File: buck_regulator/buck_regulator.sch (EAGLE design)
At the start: 12 parts

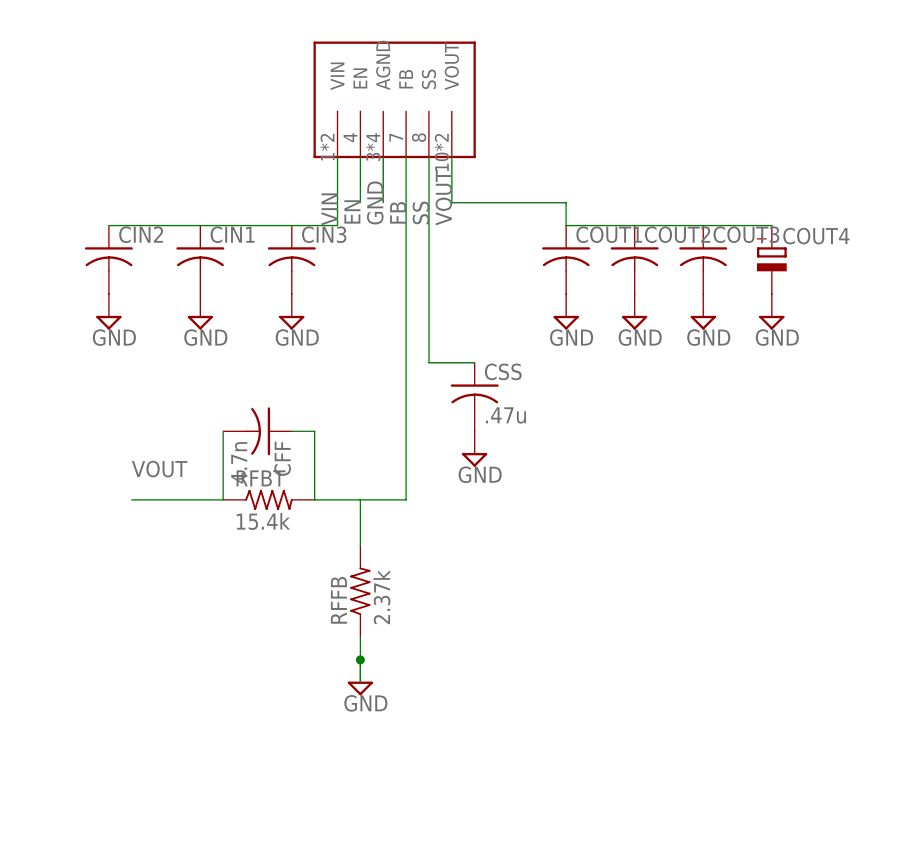
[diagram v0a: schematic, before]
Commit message: buck_regulator: re-route for revision B
Change-Id: Ie95bbfd6e64e4db471db740f6a7ad1b08f6b97fa
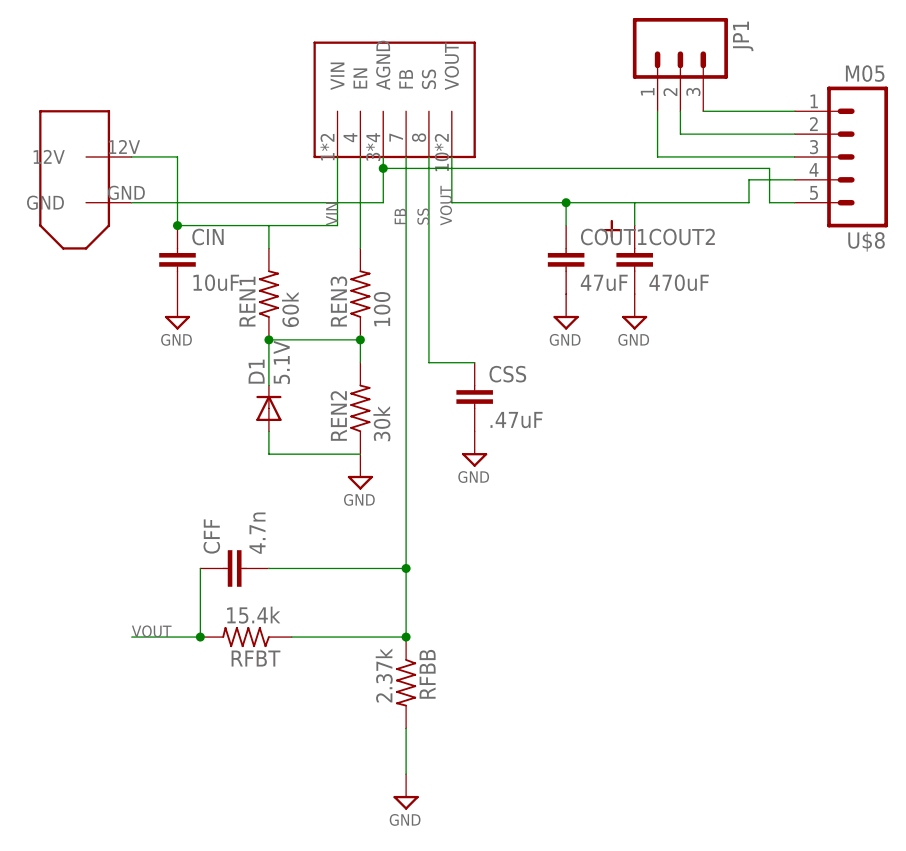
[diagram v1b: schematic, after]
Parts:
- removed CIN1, CIN2, CIN3: (no value), resistor:C-USC1206
- removed COUT3: (no value), resistor:C-USC1812K
- removed COUT4: (no value), resistor:CPOL-EU153CLV-1014
- removed RFFB: 2.37k, resistor:R-US_M0805
- added CIN: 10uF, pie:CAP0603-CAP
- added D1: 5.1V, SparkFun:DIODESOD
- added JP1: (no value), pie:M03MTA1X3
- added REN1: 60k, pie:R-US_R0603
- added REN2: 30k, pie:R-US_R0603
- added REN3: 100, pie:R-US_R0603
- added RFBB: 2.37k, pie:R-US_R0603
- added U$2: XT60CONNECTOR, pie:XT60CONNECTOR
- added U$8: M05, pie:M05
- CFF: device resistor:C-USC0805K -> pie:CAP0603-CAP
- COUT1: value (none) -> 47uF; device resistor:C-USC1206 -> SparkFun:CAP1206
- COUT2: value (none) -> 470uF; device resistor:C-USC1812K -> TANT_CASE_E:TANT_CASE_E
- CSS: value .47u -> .47uF; device resistor:C-USC0805K -> pie:CAP0603-CAP
- RFBT: device resistor:R-US_M0805 -> pie:R-US_R0603
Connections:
- removed net EN: U$1.EN
- new net N$1: REN3.2, U$1.EN
- new net N$2: JP1.1, U$8.3
- new net N$3: D1.C, REN1.1, REN2.2, REN3.1
- new net N$4: JP1.2, U$8.2
- new net N$5: JP1.3, U$8.1
- net FB: now also CFF.2, RFBB.1, RFBT.1; no longer CFF.1, RFBT.2, RFFB.2
- net GND: now also CIN.2, COUT2.NEG, D1.A, REN2.1, RFBB.2, U$2.GND, U$8.5; no longer CIN1.2, CIN2.2, CIN3.2, COUT2.2, COUT3.2, COUT4.-, RFFB.1
- net VIN: now also CIN.1, REN1.2, U$2.12V; no longer CIN1.1, CIN2.1, CIN3.1
- net VOUT: now also CFF.1, COUT2.POS, RFBT.2, U$8.4; no longer CFF.2, COUT2.1, COUT3.1, COUT4.+, RFBT.1
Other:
- moved on the sheet: CFF, RFBT

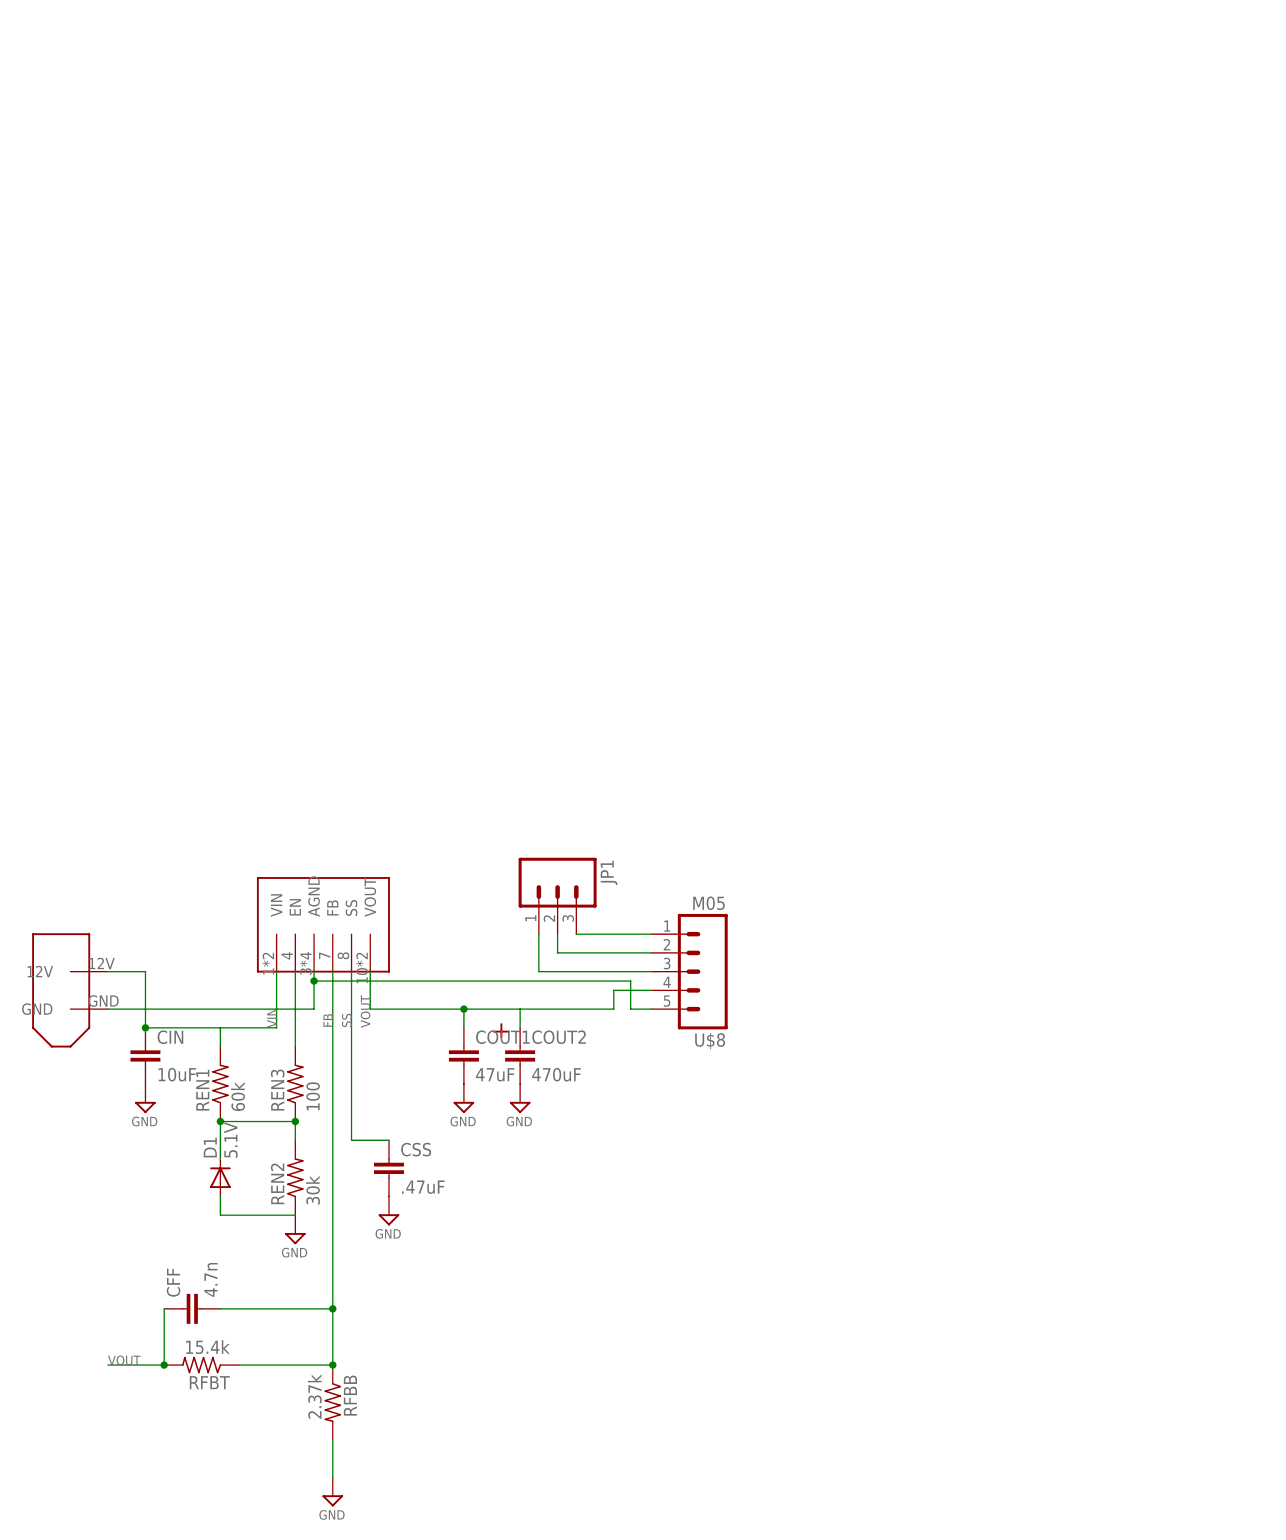
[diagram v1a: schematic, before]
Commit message: Fix all schematics to have a frame and be in quadrant I
Change-Id: I9709ffe2e940512e8f74172f888a837b658cad74
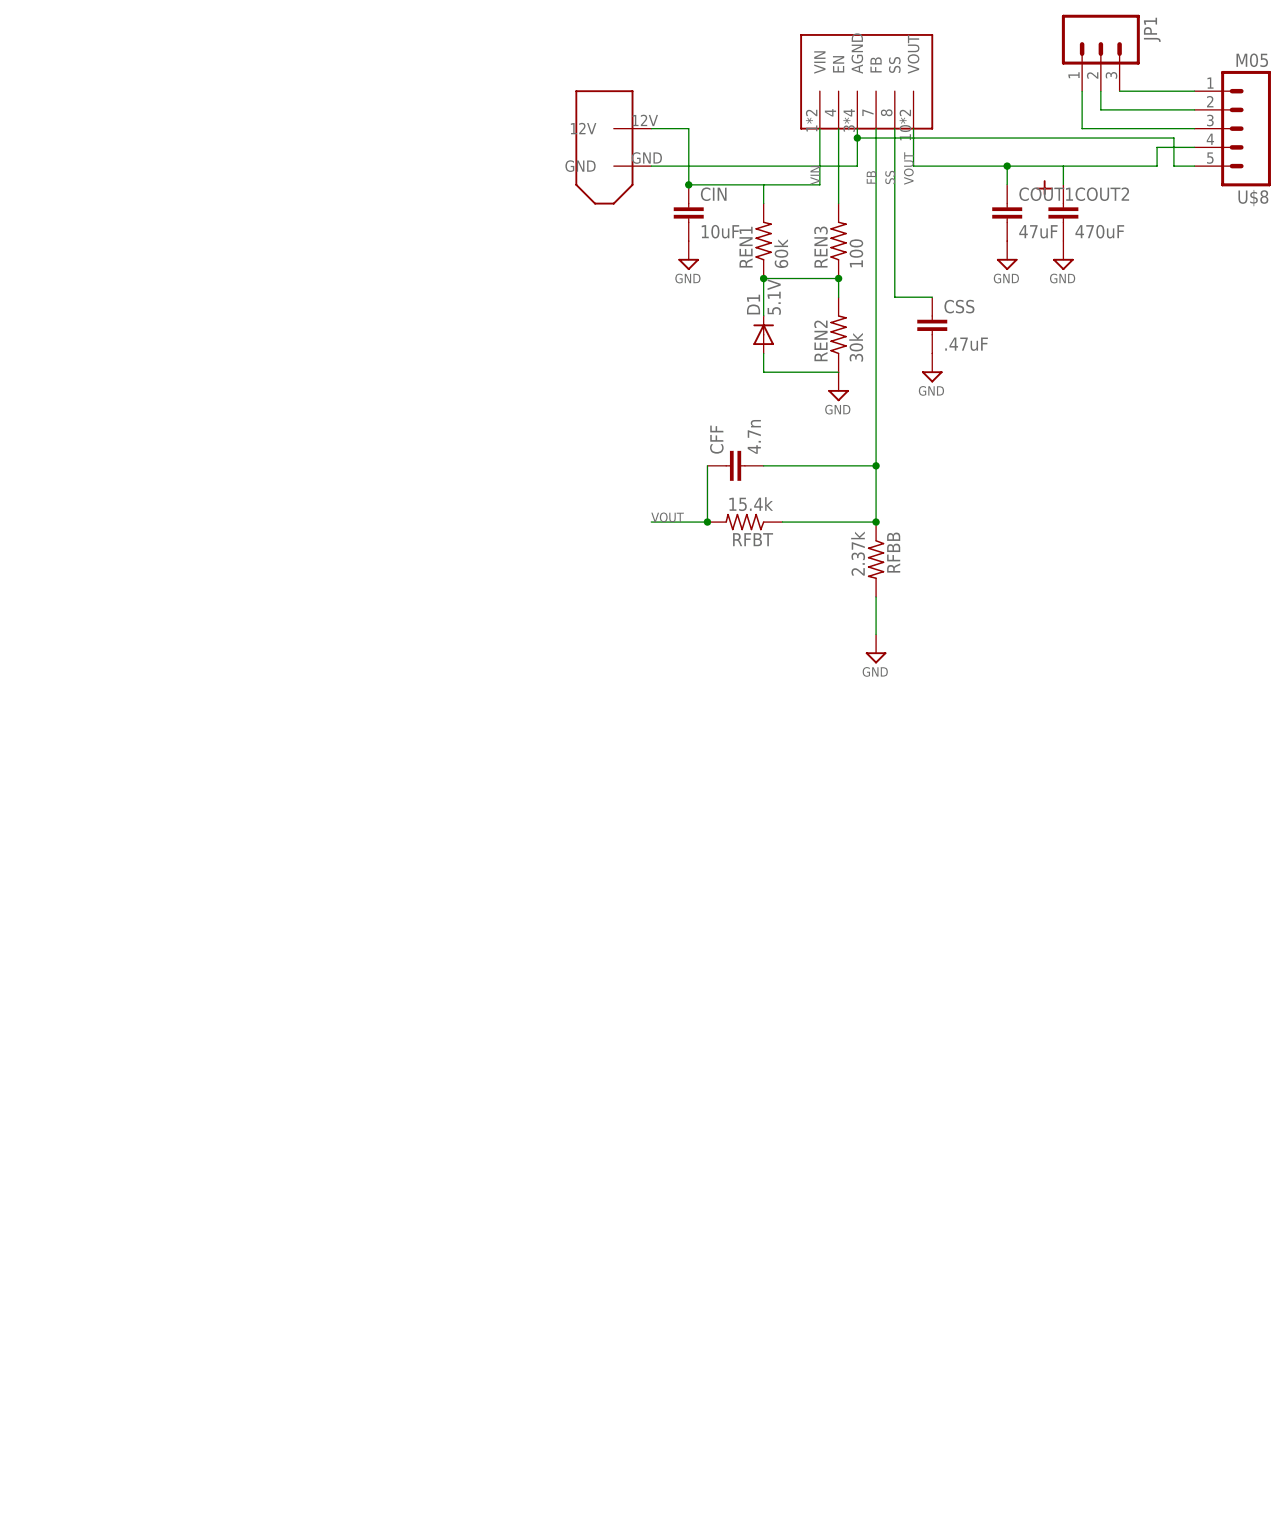
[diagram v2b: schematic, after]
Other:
- moved on the sheet: CFF, CIN, COUT1, COUT2, CSS, D1, JP1, REN1, REN2, REN3, RFBB, RFBT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
